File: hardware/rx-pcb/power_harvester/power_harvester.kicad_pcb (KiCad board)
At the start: 2 copper layers, 5 parts, among them J1 Conn_Coaxial_Small

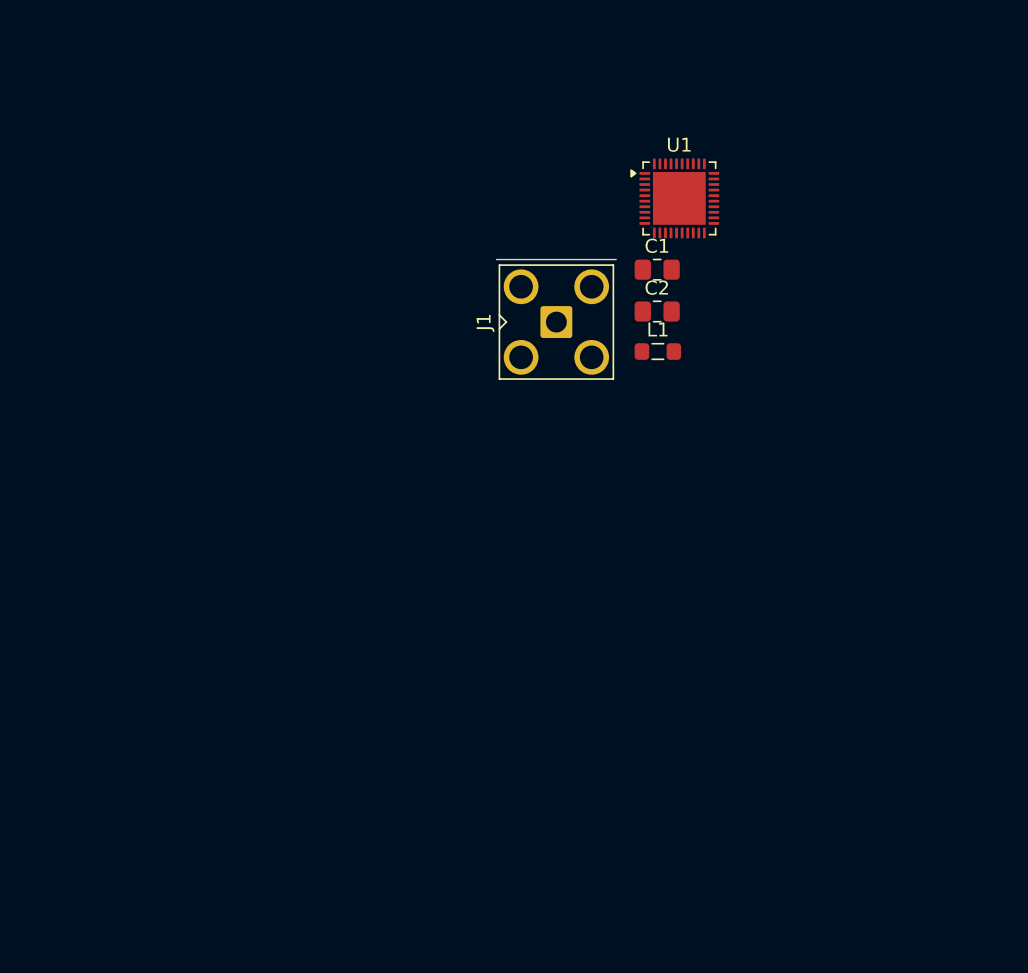
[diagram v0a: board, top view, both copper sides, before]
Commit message: added selected diodes and bank capacitor. began board layout.
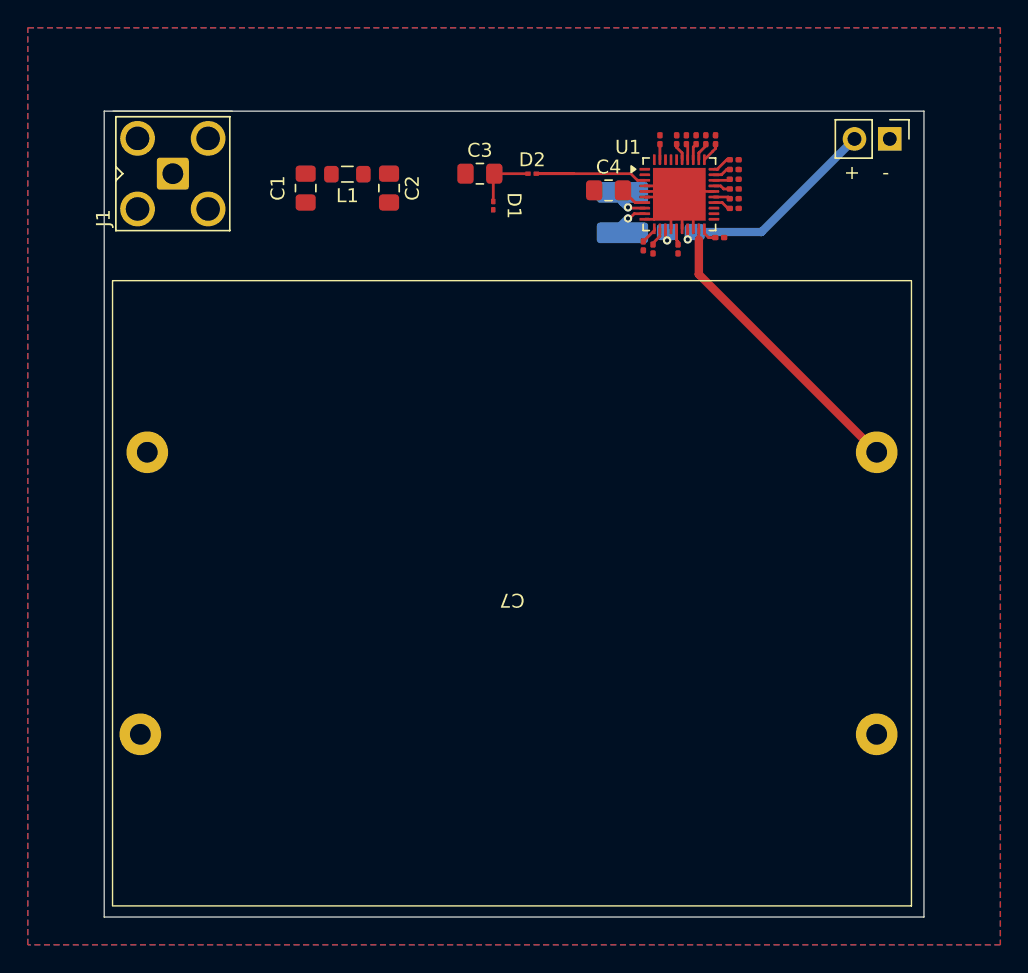
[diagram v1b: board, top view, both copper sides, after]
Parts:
- added C3: C, Capacitor_SMD:C_0805_2012Metric_Pad1.18x1.45mm_HandSolder, F.Cu at (123.5, 79.5)
- added C4: 22u, Capacitor_SMD:C_0805_2012Metric_Pad1.18x1.45mm_HandSolder, F.Cu at (132.8, 80.7)
- added C5: 10u, Capacitor_SMD:C_0805_2012Metric_Pad1.18x1.45mm_HandSolder, B.Cu at (137.0, 82.7)
- added C6: 20u, Capacitor_SMD:C_0805_2012Metric_Pad1.18x1.45mm_HandSolder, B.Cu at (139.0, 82.7)
- added C7: ~, power_harvester:C4AQXEXXXXXXXAX, F.Cu at (125.8, 109.7)
- added D1: D, power_harvester:JDH2S02SL, F.Cu at (124.5, 81.8)
- added D2: D, power_harvester:JDH2S02SL, F.Cu at (127.3, 79.5)
- added J2: Conn_01x02_Pin, Connector_PinHeader_2.54mm:PinHeader_1x02_P2.54mm_Vertical, F.Cu at (153.0, 77.0)
- added L2: 10u, power_harvester:WE-MAPI, B.Cu at (133.8, 82.3)
- added R1: on, Resistor_SMD:R_0201_0603Metric, F.Cu at (141.8, 79.9)
- added R10: off, Resistor_SMD:R_0201_0603Metric, F.Cu at (140.5, 77.1)
- added R11: off, Resistor_SMD:R_0201_0603Metric, F.Cu at (140.8, 84.1)
- added R12: off, Resistor_SMD:R_0201_0603Metric, F.Cu at (139.1, 77.1)
- added R13: off, Resistor_SMD:R_0201_0603Metric, F.Cu at (138.4, 77.1)
- added R14: off, Resistor_SMD:R_0201_0603Metric, F.Cu at (141.8, 82.0)
- added R15: off, Resistor_SMD:R_0201_0603Metric, F.Cu at (141.8, 78.5)
- added R16: off, Resistor_SMD:R_0201_0603Metric, F.Cu at (137.8, 84.9)
- added R2: on, Resistor_SMD:R_0201_0603Metric, F.Cu at (137.7, 77.1)
- added R3: on, Resistor_SMD:R_0201_0603Metric, F.Cu at (141.8, 80.6)
- added R4: on, Resistor_SMD:R_0201_0603Metric, F.Cu at (141.8, 81.3)
- added R5: on, Resistor_SMD:R_0201_0603Metric, F.Cu at (139.8, 77.1)
- added R6: on, Resistor_SMD:R_0201_0603Metric, F.Cu at (136.0, 84.9)
- added R7: on, Resistor_SMD:R_0201_0603Metric, F.Cu at (135.3, 84.7)
- added R8: off, Resistor_SMD:R_0201_0603Metric, F.Cu at (136.5, 77.1)
- added R9: off, Resistor_SMD:R_0201_0603Metric, F.Cu at (141.8, 79.2)
- moved J1 29.6 mm to (101.4, 79.5)
- moved C1 26.0 mm to (111.0, 80.5), turned to -90 degrees
- moved L1 25.7 mm to (114.0, 79.5), turned to 180 degrees
- moved C2 21.2 mm to (117.0, 80.5), turned to -90 degrees
- moved U1 0.30 mm to (137.9, 81.0)
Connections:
- U1 pad 1: unconnected-(U1-CS_in-Pad1) -> /Pin
- U1 pad 10: unconnected-(U1-GND-Pad10) -> GND
- U1 pad 11: unconnected-(U1-R_MPP[2]-Pad11) -> Net-(U1-R_MPP[2])
- U1 pad 12: unconnected-(U1-R_MPP[1]-Pad12) -> Net-(U1-R_MPP[1])
- U1 pad 13: unconnected-(U1-VINT-Pad13) -> /Vint
- U1 pad 14: unconnected-(U1-GND-Pad14) -> GND
- U1 pad 15: unconnected-(U1-R_MPP[0]-Pad15) -> Net-(U1-R_MPP[0])
- U1 pad 16: unconnected-(U1-GND-Pad16) -> GND
- U1 pad 17: unconnected-(U1-LOAD-Pad17) -> /Po
- U1 pad 18: unconnected-(U1-BAL-Pad18) -> GND
- U1 pad 19: unconnected-(U1-STO-Pad19) -> /bank
- U1 pad 20: unconnected-(U1-EN_STO_CH-Pad20) -> Net-(U1-EN_STO_CH)
- U1 pad 24: unconnected-(U1-LOAD_CFG[0]-Pad24) -> Net-(U1-LOAD_CFG[0])
- U1 pad 25: unconnected-(U1-LOAD_CFG[1]-Pad25) -> Net-(U1-LOAD_CFG[1])
- U1 pad 26: unconnected-(U1-GND-Pad26) -> GND
- U1 pad 27: unconnected-(U1-STO_CFG[3]-Pad27) -> Net-(U1-STO_CFG[3])
- U1 pad 28: unconnected-(U1-EN_HP-Pad28) -> Net-(U1-EN_HP)
- U1 pad 29: unconnected-(U1-STO_PRIO-Pad29) -> Net-(U1-STO_PRIO)
- U1 pad 3: unconnected-(U1-SRC-Pad3) -> /Pin
- U1 pad 30: unconnected-(U1-T_MPP[0]-Pad30) -> Net-(U1-T_MPP[0])
- U1 pad 31: unconnected-(U1-EN_STO_FT-Pad31) -> Net-(U1-EN_STO_FT)
- U1 pad 32: unconnected-(U1-T_MPP[1]-Pad32) -> Net-(U1-T_MPP[1])
- U1 pad 33: unconnected-(U1-STO_CFG[0]-Pad33) -> Net-(U1-STO_CFG[0])
- U1 pad 34: unconnected-(U1-STO_CFG[1]-Pad34) -> Net-(U1-STO_CFG[1])
- U1 pad 35: unconnected-(U1-STO_CFG[2]-Pad35) -> Net-(U1-STO_CFG[2])
- U1 pad 39: unconnected-(U1-EN_SLEEP-Pad39) -> Net-(U1-EN_SLEEP)
- U1 pad 4: unconnected-(U1-GND-Pad4) -> GND
- U1 pad 41: unconnected-(U1-GND-Pad41) -> GND
- U1 pad 5: unconnected-(U1-GND-Pad5) -> GND
- U1 pad 6: unconnected-(U1-GND-Pad6) -> GND
- U1 pad 7: unconnected-(U1-BUFSRC-Pad7) -> Net-(U1-BUFSRC)
- U1 pad 8: unconnected-(U1-Lin-Pad8) -> Net-(U1-Lin)
- U1 pad 9: unconnected-(U1-Lout-Pad9) -> Net-(U1-Lout)
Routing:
- net GND: track 0.00 -> 21.9 mm
- net /bank: track 0.00 -> 21.4 mm
- net /Po: track 0.00 -> 15.8 mm, vias 0 -> 1
- net /Pin: track 0.00 -> 10.7 mm
- net Net-(D1-K): track 0.00 -> 4.46 mm
- net Net-(U1-Lout): track 0.00 -> 3.31 mm, vias 0 -> 1
- net Net-(U1-Lin): track 0.00 -> 2.68 mm, vias 0 -> 1
- net Net-(U1-BUFSRC): track 0.00 -> 1.93 mm
- net Net-(U1-EN_STO_FT): track 0.00 -> 1.45 mm
- net Net-(U1-T_MPP[0]): track 0.00 -> 1.42 mm
- net Net-(U1-R_MPP[1]): track 0.00 -> 1.34 mm
- net Net-(U1-T_MPP[1]): track 0.00 -> 1.33 mm
- net Net-(U1-LOAD_CFG[0]): track 0.00 -> 1.32 mm
- net Net-(U1-STO_PRIO): track 0.00 -> 1.30 mm
- net Net-(U1-STO_CFG[2]): track 0.00 -> 1.28 mm
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- added copper zone on B.Cu, net GND
- added copper zone on F.Cu, net GND
- added copper zone on In1.Cu, net GND
- added copper zone on In2.Cu, net GND
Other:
- board outline added: 59 x 58 mm
- copper layers 2 -> 4
- board text added: "+"
- board text added: "-"

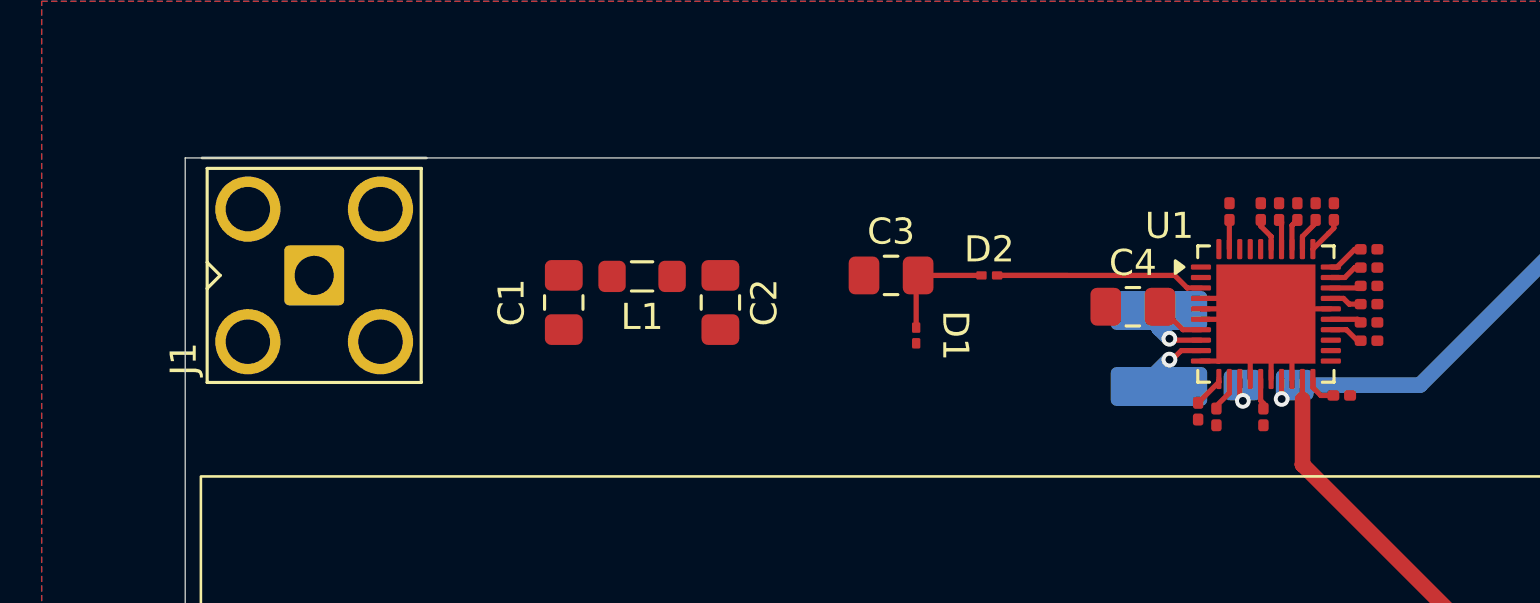
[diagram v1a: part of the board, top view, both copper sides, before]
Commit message: updated harvester PCB with reverse voltage suppression diodes.
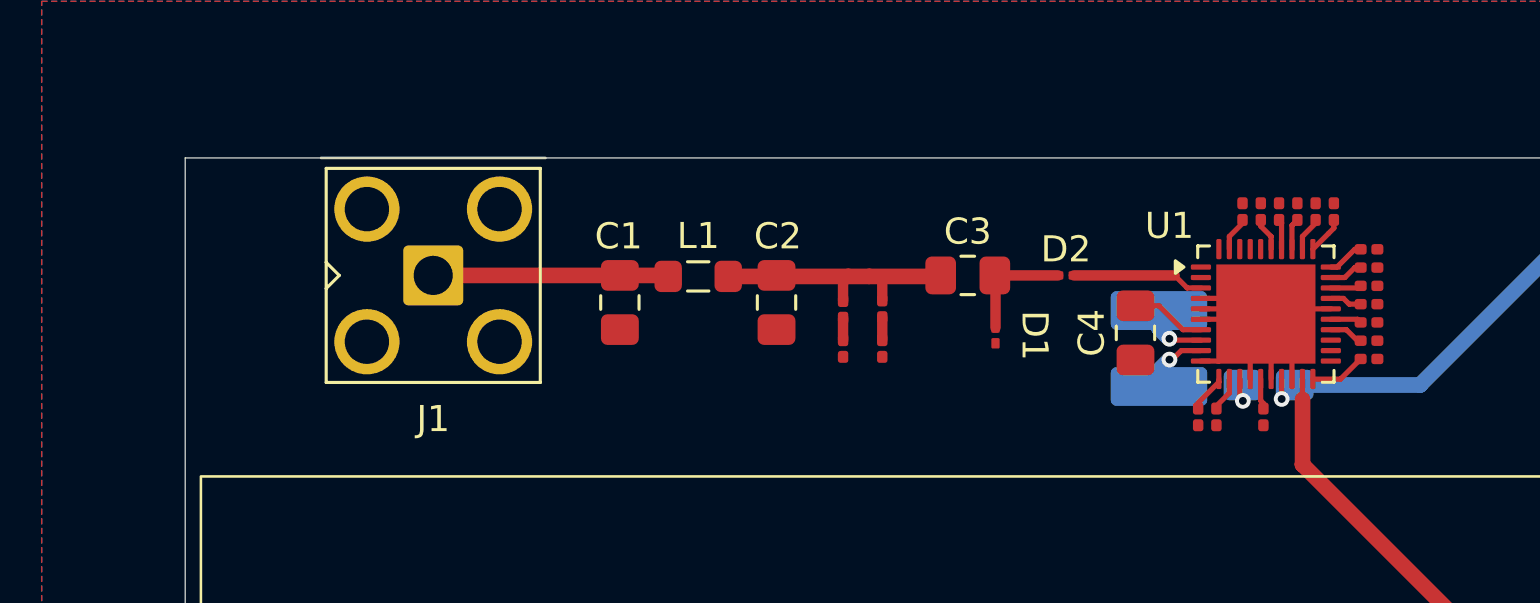
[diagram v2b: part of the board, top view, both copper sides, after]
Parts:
- added D3: D_Zener, Capacitor_SMD:C_0201_0603Metric, F.Cu at (121.7, 80.8)
- added D4: D_Zener, Capacitor_SMD:C_0201_0603Metric, F.Cu at (121.7, 82.3)
- added D5: D_Zener, Capacitor_SMD:C_0201_0603Metric, F.Cu at (123.2, 80.8)
- added D6: D_Zener, Capacitor_SMD:C_0201_0603Metric, F.Cu at (123.2, 82.3)
- moved J1 4.56 mm to (106.0, 79.5)
- moved D1 3.04 mm to (127.5, 81.8)
- moved D2 2.94 mm to (130.2, 79.5)
- moved C3 2.94 mm to (126.5, 79.5)
- moved C1 2.15 mm to (113.2, 80.5)
- moved C2 2.15 mm to (119.2, 80.5)
- moved L1 2.15 mm to (116.2, 79.5), turned to 0 degrees
- moved R11 1.75 mm to (141.8, 82.7)
- moved C4 1.00 mm to (132.9, 81.7), turned to 90 degrees
- moved R8 0.50 mm to (137.0, 77.1)
- moved R7 0.22 mm to (135.3, 84.9)
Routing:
- net Net-(D3-K): track 0.00 -> 10.0 mm
- net Net-(J1-In): track 0.00 -> 9.02 mm
- net /Pin: track 10.7 -> 5.07 mm
- net Net-(U1-BUFSRC): track 1.93 -> 2.89 mm
- net Net-(U1-EN_STO_CH): track 1.24 -> 2.15 mm
- net Net-(D5-A): track 0.00 -> 0.88 mm
- net Net-(D3-A): track 0.00 -> 0.86 mm

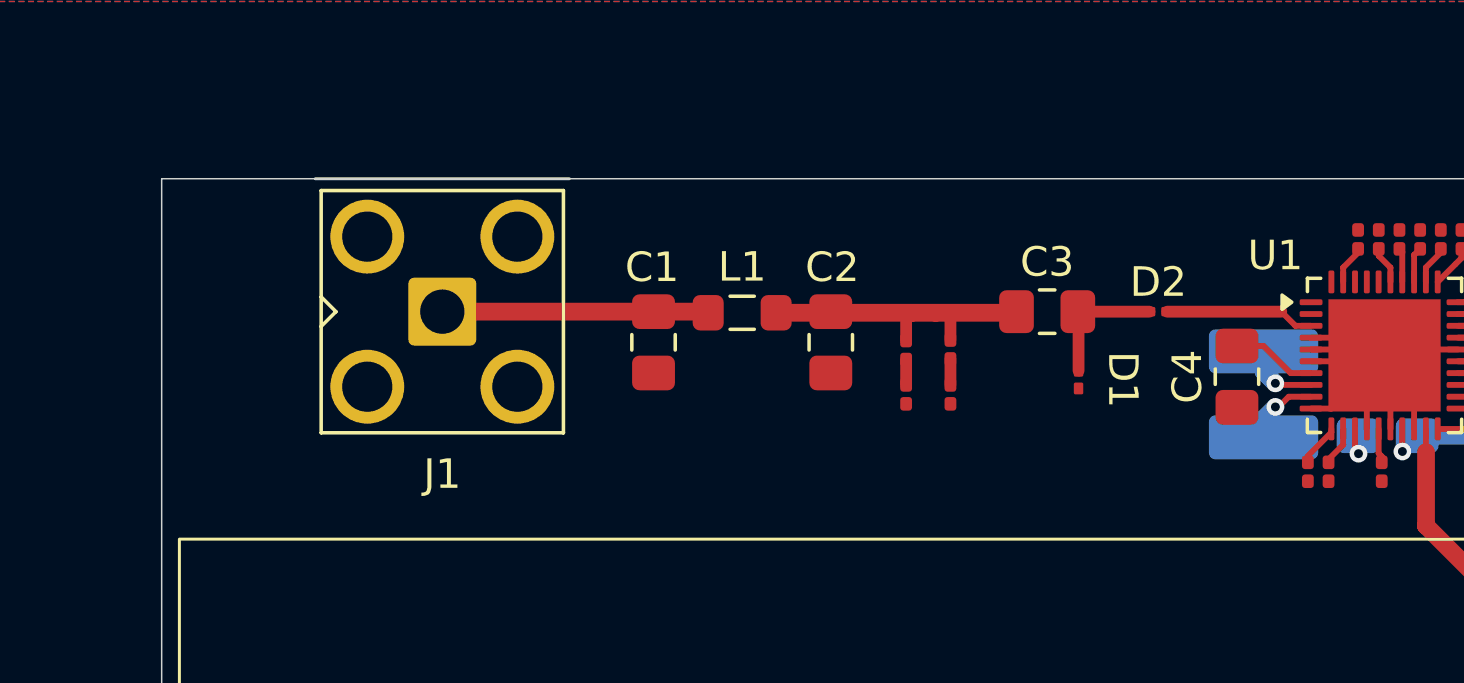
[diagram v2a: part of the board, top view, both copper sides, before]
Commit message: updated harvester with compartmentalization testing resistors and test points. updated bluetooth test to use a low Vf diode rather than an LED for reverse current protection. must update footprint for that.
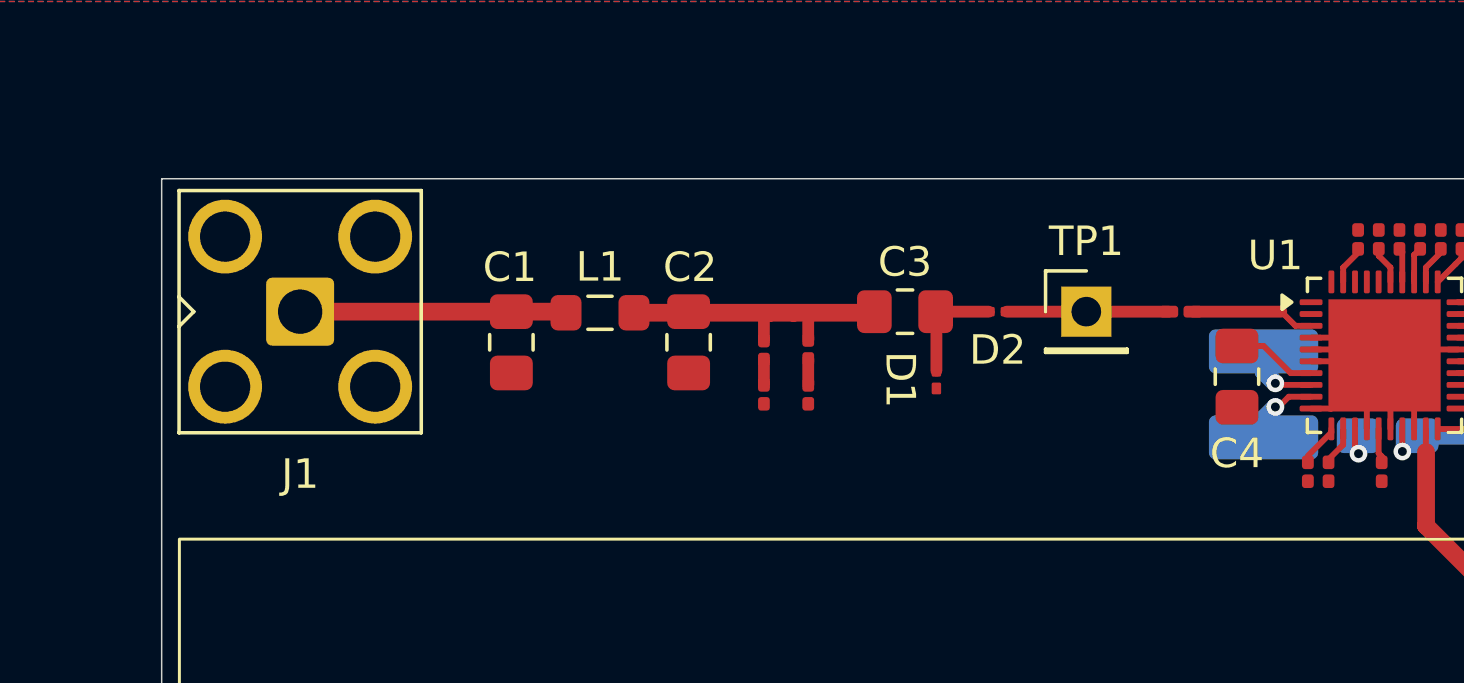
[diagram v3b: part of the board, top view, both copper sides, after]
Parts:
- added R17: 0, Resistor_SMD:R_0201_0603Metric_Pad0.64x0.40mm_HandSolder, F.Cu at (131.0, 79.5)
- added TP1: Conn_01x01_Pin, Connector_PinHeader_2.54mm:PinHeader_1x01_P2.54mm_Vertical, F.Cu at (127.8, 79.5)
- moved D2 5.44 mm to (124.8, 79.5)
- moved C1 4.81 mm to (108.3, 80.5)
- moved C2 4.81 mm to (114.3, 80.5)
- moved C3 4.81 mm to (121.7, 79.5)
- moved D1 4.81 mm to (122.7, 81.8)
- moved D3 4.81 mm to (116.9, 80.8)
- moved D4 4.81 mm to (116.9, 82.3)
- moved D5 4.81 mm to (118.4, 80.8)
- moved D6 4.81 mm to (118.4, 82.3)
- moved J1 4.81 mm to (101.2, 79.5)
- moved L1 4.81 mm to (111.3, 79.5)
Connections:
- D2 pad 1: /Pin -> Net-(D2-K)
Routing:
- net Net-(D2-K): track 0.00 -> 5.49 mm
- net /Pin: track 5.07 -> 4.20 mm
- net Net-(D1-K): track 4.44 -> 3.81 mm

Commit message: power harvester updates and cleanup
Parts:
- removed D5, D6: D_Zener, Capacitor_SMD:C_0201_0603Metric
- removed TP1: Conn_01x01_Pin, Connector_PinHeader_2.54mm:PinHeader_1x01_P2.54mm_Vertical
- added C10: C, Capacitor_SMD:C_0603_1608Metric_Pad1.08x0.95mm_HandSolder, F.Cu at (113.8, 87.3)
- added C8: 22u, Capacitor_SMD:C_0603_1608Metric_Pad1.08x0.95mm_HandSolder, F.Cu at (127.8, 86.2)
- added C9: C, Capacitor_SMD:C_0603_1608Metric_Pad1.08x0.95mm_HandSolder, F.Cu at (105.4, 87.3)
- added J3: Conn_Coaxial_Small, Connector_PinHeader_2.54mm:PinHeader_1x02_P2.54mm_Vertical, F.Cu at (118.5, 76.8)
- added J4: Conn_Coaxial_Small, Connector_PinHeader_2.54mm:PinHeader_1x02_P2.54mm_Vertical, F.Cu at (130.1, 76.8)
- added L3: L, Inductor_SMD:L_0805_2012Metric_Pad1.05x1.20mm_HandSolder, F.Cu at (109.6, 84.5)
- added R18: 0, Resistor_SMD:R_0201_0603Metric_Pad0.64x0.40mm_HandSolder, F.Cu at (118.1, 85.3)
- added R19: 0, Resistor_SMD:R_0201_0603Metric_Pad0.64x0.40mm_HandSolder, F.Cu at (118.5, 83.2)
- added R20: 0, Resistor_SMD:R_0201_0603Metric_Pad0.64x0.40mm_HandSolder, F.Cu at (130.1, 83.1)
- C1, C2, C4, C5, C6: footprint Capacitor_SMD:C_0805_2012Metric_Pad1.18x1.45mm_HandSolder -> Capacitor_SMD:C_0603_1608Metric_Pad1.08x0.95mm_HandSolder
- C3: value C -> 1n; footprint Capacitor_SMD:C_0805_2012Metric_Pad1.18x1.45mm_HandSolder -> Capacitor_SMD:C_0603_1608Metric_Pad1.08x0.95mm_HandSolder
- C7: moved to B.Cu
- moved C7 11.2 mm to (125.8, 98.5)
- moved R6 8.90 mm to (142.8, 90.7)
- moved C5 8.63 mm to (143.4, 88.5)
- moved C6 8.63 mm to (145.4, 88.5)
- moved R3 8.63 mm to (148.2, 86.4)
- moved R1 8.63 mm to (148.2, 85.7)
- moved R10 8.63 mm to (146.9, 82.9)
- moved R11 8.63 mm to (148.2, 88.5)
- moved R12 8.63 mm to (145.5, 82.9)
- moved R14 8.63 mm to (148.2, 87.8)
- moved R15 8.63 mm to (148.2, 84.3)
- moved R2 8.63 mm to (144.1, 82.9)
- moved R4 8.63 mm to (148.2, 87.1)
- moved R8 8.63 mm to (143.4, 82.9)
- moved R9 8.63 mm to (148.2, 85.0)
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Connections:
- C1 pad 2: GND -> Net-(C1-Pad2)
- C2 pad 2: GND -> Net-(C10-Pad1)
- C3 pad 1: Net-(D3-K) -> Net-(C3-Pad1)
- L1 pad 1: Net-(J1-In) -> Net-(D3-K)
- L1 pad 2: Net-(D3-K) -> Net-(J1-In)
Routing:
- net /bank: track 21.4 -> 49.5 mm
- net Net-(J3-In): track 0.00 -> 5.99 mm
- net Net-(J4-In): track 0.00 -> 5.89 mm
- net Net-(D2-K): track 5.49 -> 9.69 mm
- net Net-(C3-Pad1): track 0.00 -> 3.90 mm
- net /Pin: track 4.20 -> 7.96 mm
- net Net-(J1-In): track 9.02 -> 12.8 mm
- net Net-(C10-Pad1): track 0.00 -> 1.50 mm
- net Net-(C1-Pad2): track 0.00 -> 1.50 mm
- net /Vint: track 0.69 -> 1.80 mm
- net Net-(D3-K): track 10.0 -> 9.04 mm
- net Net-(D5-A): track 0.88 -> 0.00 mm
- net /Po: track 15.8 -> 16.3 mm
- net GND: vias 0 -> 3
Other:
- board size 59 x 58 mm -> 59 x 46.8 mm
